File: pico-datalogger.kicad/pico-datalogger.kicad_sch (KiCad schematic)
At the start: 35 parts, among them J1 JST-PH2 VCC, J10 Conn_Inky_SW, J11 I2C_1, J12 I2C_7, J14 I2C_6, J16 BG_2, J18 I2C_5, J19 I2C_4, J2 I2C_8, J20 BG_3, J3 RFM9x_Lora_Breakout, J4 Alt-VCC, J5 Conn_I2S, J6 Conn_Inky_SPI, J7 Micro_SD_TF_PUSH, J8 Conn_ADC, J9 Conn_UART, SW1 SW_Push_SLIM, SW2 SW_Reset, U1 SN74HC74N, U2 PCF8523T, U3 Pico, Y1 Crystal

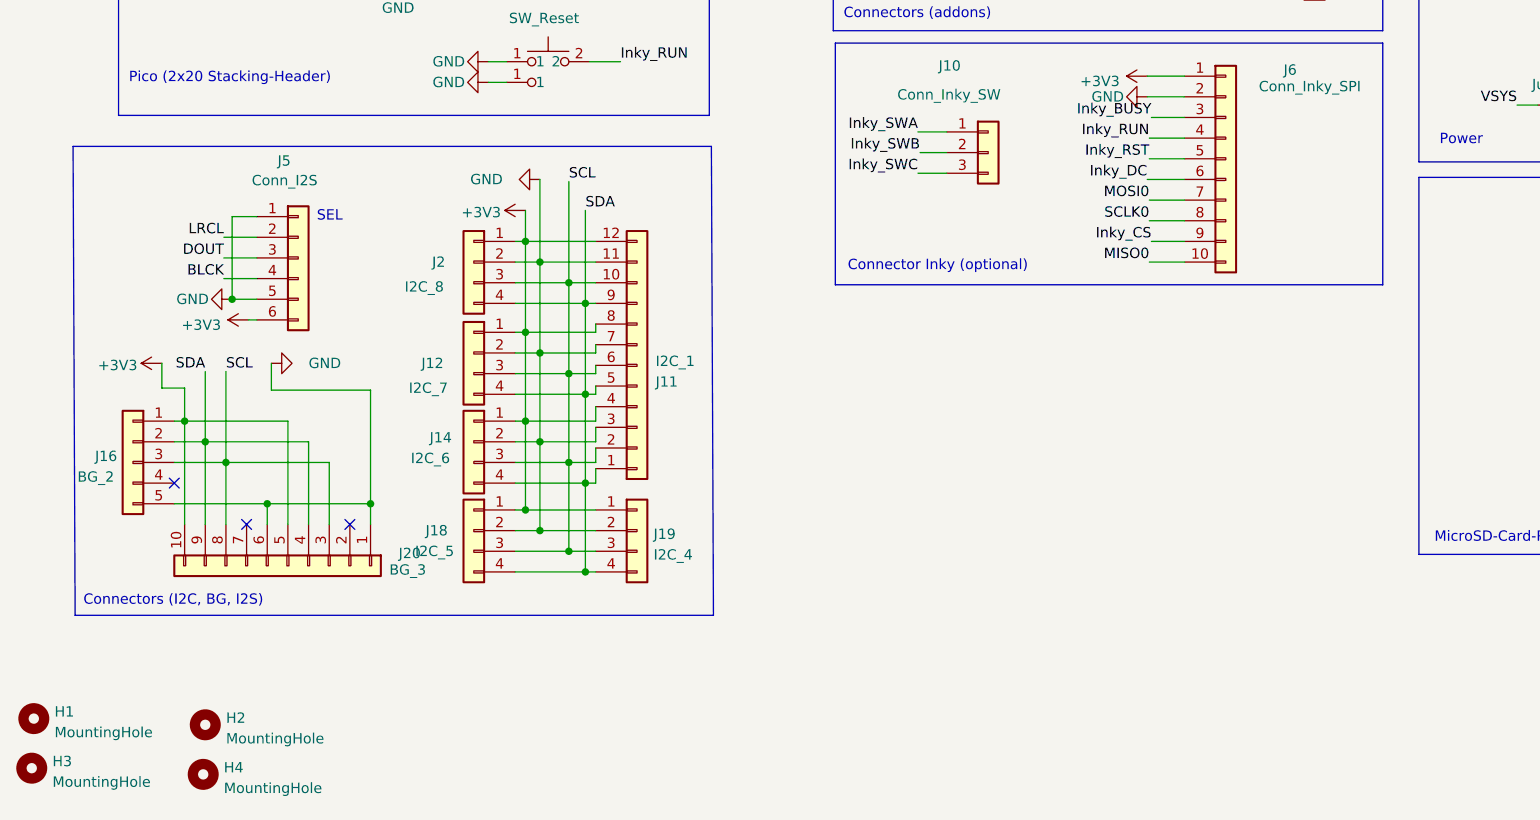
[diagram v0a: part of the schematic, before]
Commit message: Rev 1.00: fix Stemma/Qt connectors
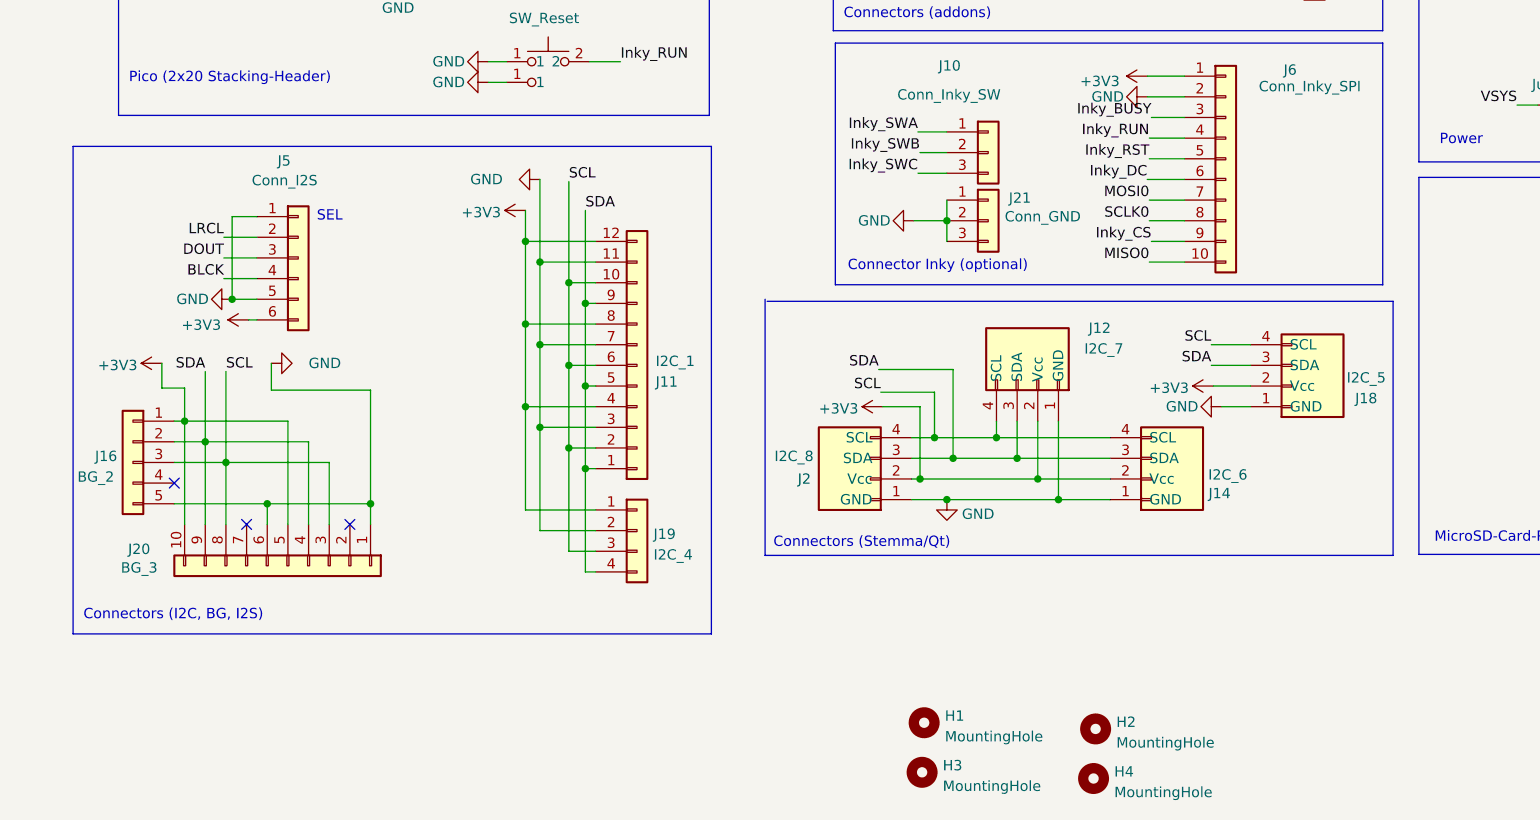
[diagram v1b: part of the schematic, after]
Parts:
- added J21: Conn_GND, Connector_PinHeader_2.54mm:PinHeader_1x03_P2.54mm_Vertical, symbol Connector_Generic:Conn_01x03
- J12, J14, J18, J2: symbol Connector_Generic:Conn_01x04 -> user:Stemma-QT_Qwicc
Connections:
- net +3V3: now also J12.2 (Vcc), J14.2 (Vcc), J18.2 (Vcc), J2.2 (Vcc); no longer J12.1 (Pin_1), J14.1 (Pin_1), J18.1 (Pin_1), J2.1 (Pin_1)
- net GND: now also J12.1 (GND), J14.1 (GND), J18.1 (GND), J2.1 (GND), J21.1 (Pin_1), J21.2 (Pin_2), J21.3 (Pin_3); no longer J12.2 (Pin_2), J14.2 (Pin_2), J18.2 (Pin_2), J2.2 (Pin_2)
- net SCL: now also J12.4 (SCL), J14.4 (SCL), J18.4 (SCL), J2.4 (SCL); no longer J12.3 (Pin_3), J14.3 (Pin_3), J18.3 (Pin_3), J2.3 (Pin_3)
- net SDA: now also J12.3 (SDA), J14.3 (SDA), J18.3 (SDA), J2.3 (SDA); no longer J12.4 (Pin_4), J14.4 (Pin_4), J18.4 (Pin_4), J2.4 (Pin_4)
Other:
- note added: "Connectors (Stemma/Qt)"
- moved on the sheet: H1, H2, H3, H4
